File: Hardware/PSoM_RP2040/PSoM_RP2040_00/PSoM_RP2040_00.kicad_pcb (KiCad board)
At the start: 6 copper layers, 26.3 x 23.2 mm, 54 parts, among them J201 Bare PCB USB C, J202 DF40C-60DP-0.4V(51), SW501 SW_Push, SW502 SW_Push, U301 BQ24075RGTR, U401 MIC5528-3.3YMT-T5, U501 SC0914_7_, U502 W25Q128JVPIQ_TR, Y501 830105420809

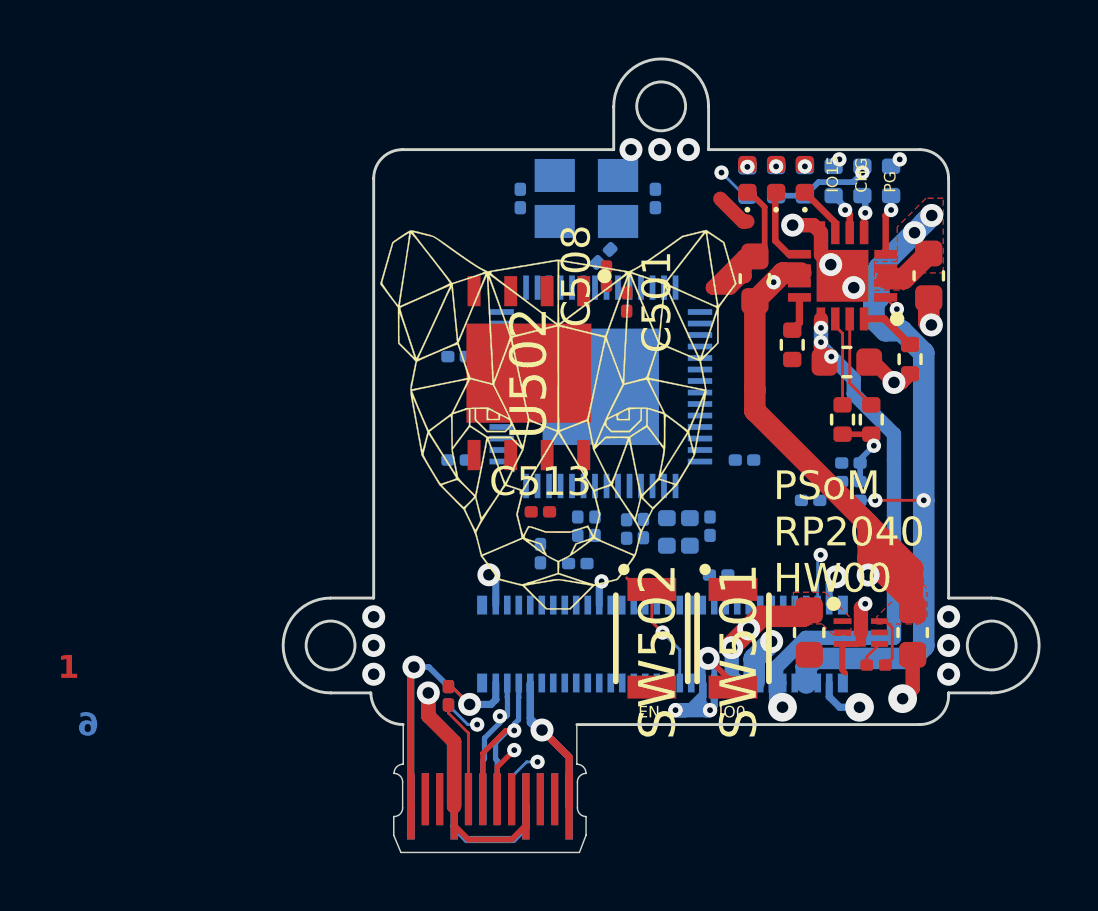
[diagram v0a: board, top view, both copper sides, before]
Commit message: small adjustements on rp2040 routing
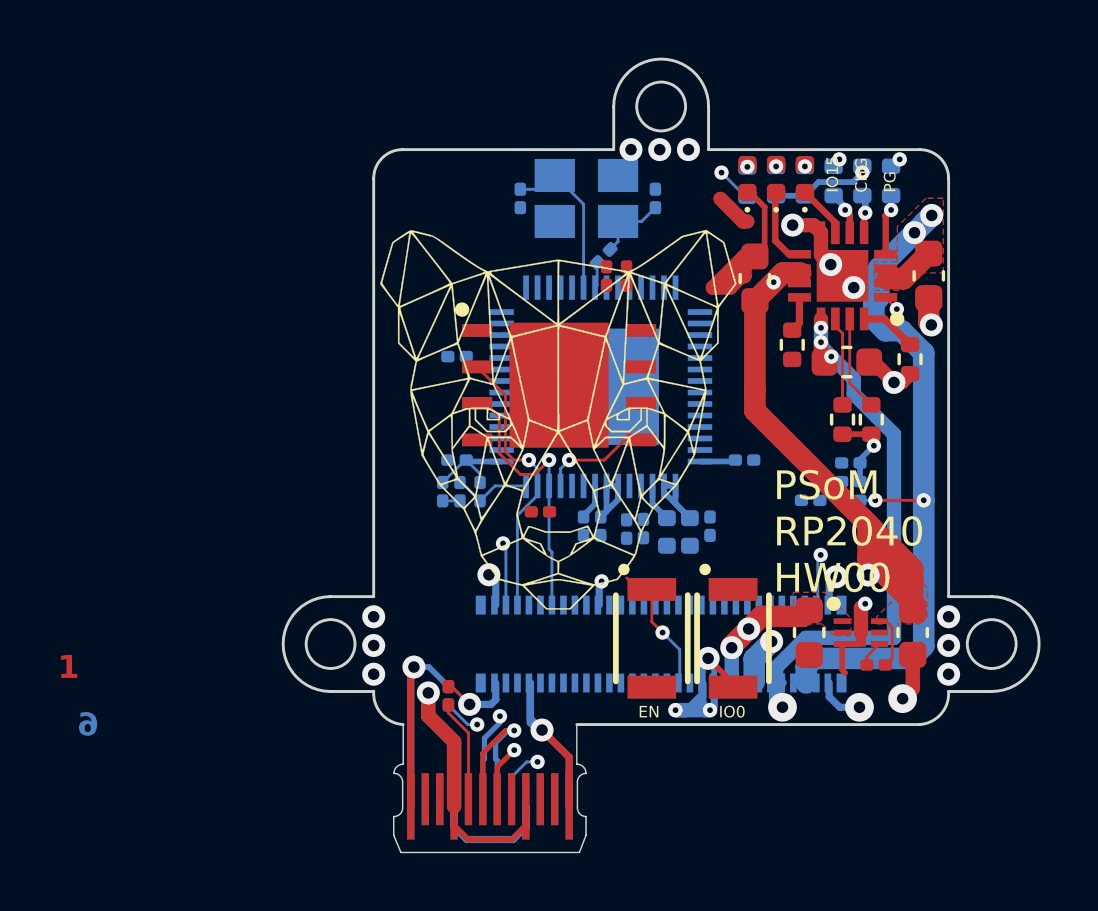
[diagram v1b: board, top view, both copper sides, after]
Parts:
- moved R507 10.0 mm to (128.4, 100.9), turned to -90 degrees
- moved R503 4.80 mm to (129.0, 100.9), turned to -90 degrees
- moved R504 3.01 mm to (129.7, 100.9)
- moved U502 1.13 mm to (132.4, 97.2), turned to 0 degrees
- moved C501 0.90 mm to (134.8, 93.4), turned to 90 degrees
- moved C502 0.20 mm to (133.3, 102.1)
- moved C507 0.20 mm to (133.9, 102.1)
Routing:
- net +3V3: track 5.66 -> 16.4 mm
- net SPI1: track 0.00 -> 9.75 mm, vias 0 -> 1
- net SPI4: track 0.00 -> 9.56 mm, vias 0 -> 1
- net SPI0: track 0.00 -> 6.00 mm, vias 0 -> 2
- net /500_RP2040/XIN: track 0.00 -> 5.71 mm
- net SPI3: track 0.00 -> 2.78 mm
- net Net-(C511-Pad1): track 0.00 -> 2.59 mm
- net +1V1: track 0.00 -> 2.57 mm
- net /200_Connectors/D+: track 7.55 -> 5.83 mm
- net /200_Connectors/D-: track 7.88 -> 6.48 mm
- net /500_RP2040/XOUT: track 0.00 -> 0.90 mm
- net /200_Connectors/BOOT0: track 0.00 -> 0.60 mm
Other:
- outline, holes or cut-outs redrawn
